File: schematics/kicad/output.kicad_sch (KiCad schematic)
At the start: 33 parts, among them J7 DE15_Socket_HighDensity, K1300 10uF, U1 BT458, U1300 HM53461, U1301 HM53461, U1302 HM53461, U1303 HM53461, U1304 HM53461, U1305 HM53461, U1306 HM53461, U1307 HM53461, U1311 92.9405Mhz, U1314 10H350, U1315 LM385BZ-1.2, U1318 74F08, U2 10H101, U3 10H131

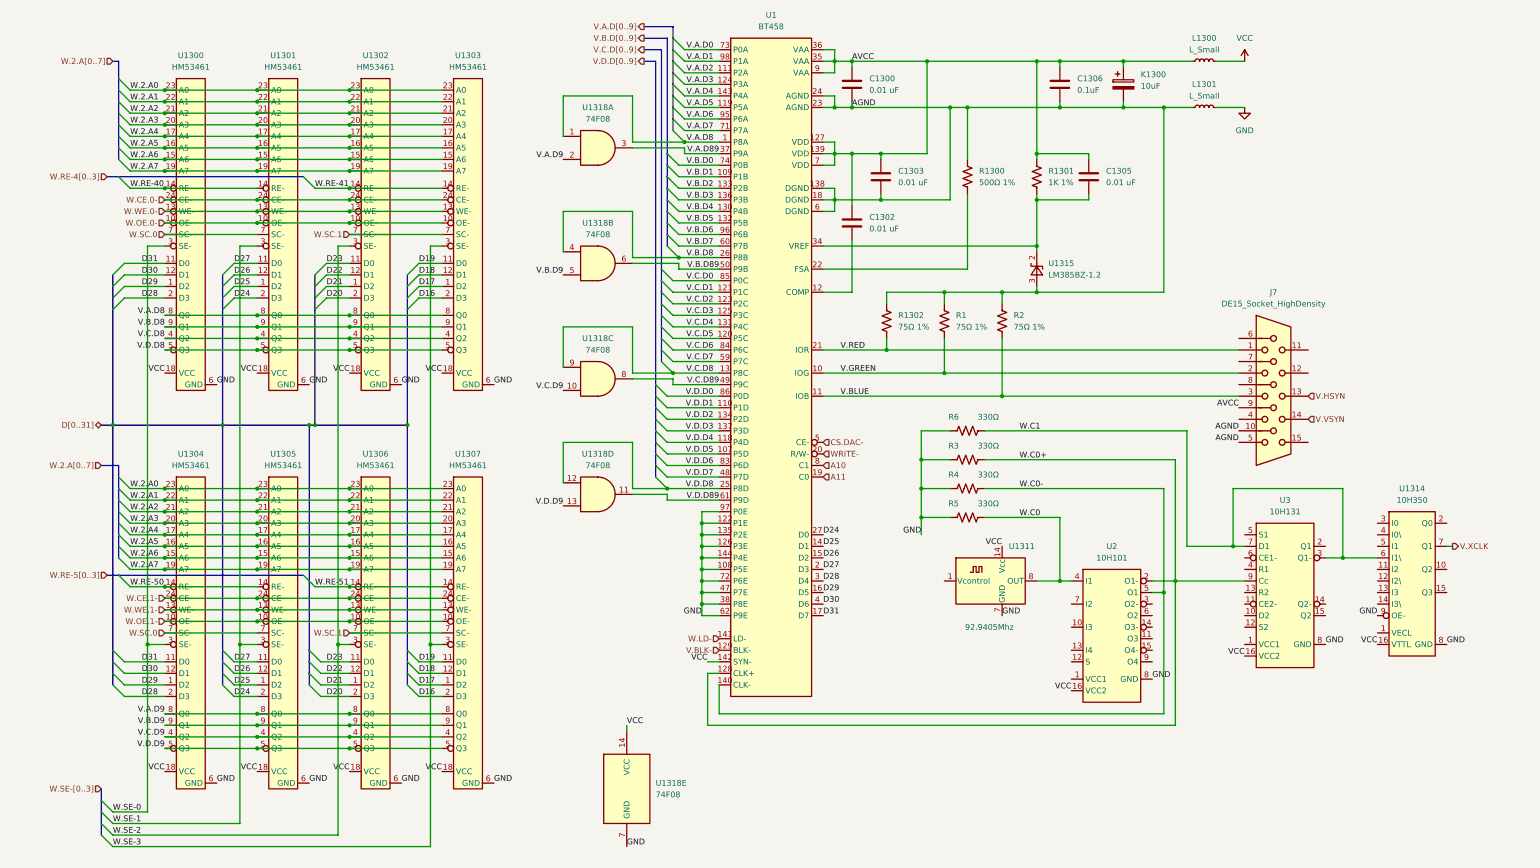
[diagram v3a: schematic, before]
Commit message: First initial layout, fix ZIP footprint.
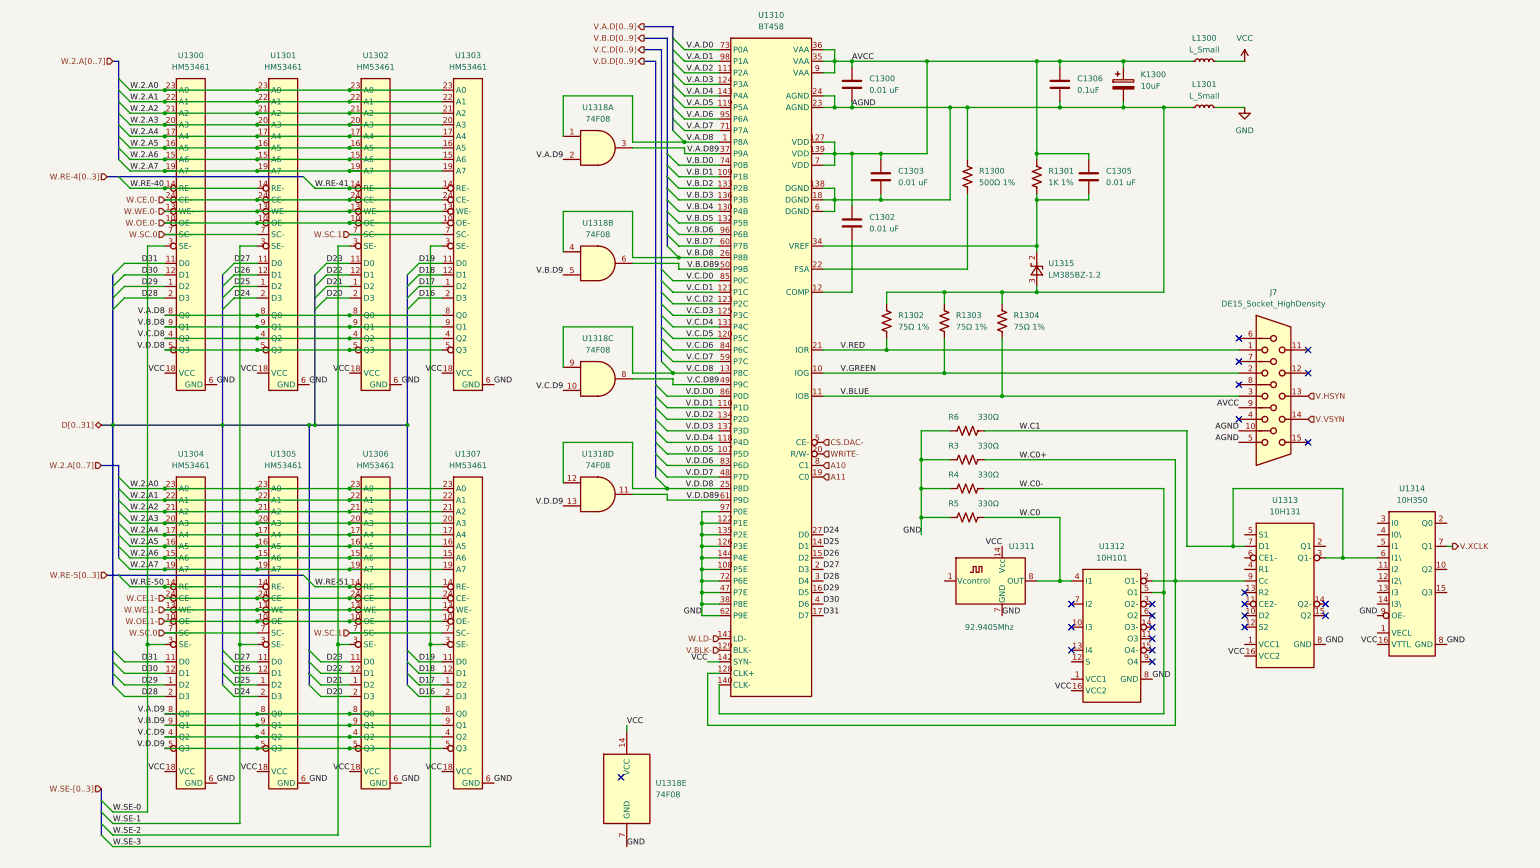
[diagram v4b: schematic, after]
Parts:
- C1300, C1302, C1303, C1305, C1306: footprint (none) -> Capacitor_THT:C_Rect_L7.0mm_W2.0mm_P5.00mm
- J7: footprint (none) -> Connector_Dsub:DSUB-15-HD_Socket_Horizontal_P2.29x2.54mm_EdgePinOffset8.35mm_Housed_MountingHolesOffset10.89mm
- K1300: footprint (none) -> Capacitor_THT:CP_Radial_D10.0mm_P5.00mm
- L1300, L1301: footprint (none) -> Resistor_THT:R_Axial_DIN0309_L9.0mm_D3.2mm_P12.70mm_Horizontal
- R1300, R1301, R1302, R3, R4, R5, R6: footprint (none) -> Resistor_THT:R_Axial_DIN0207_L6.3mm_D2.5mm_P10.16mm_Horizontal
- R1303: renamed from R1; footprint (none) -> Resistor_THT:R_Axial_DIN0207_L6.3mm_D2.5mm_P10.16mm_Horizontal
- R1304: renamed from R2; footprint (none) -> Resistor_THT:R_Axial_DIN0207_L6.3mm_D2.5mm_P10.16mm_Horizontal
- U1318: footprint (none) -> Package_DIP:DIP-14_W7.62mm
- renumbered U1 to U1310, U2 to U1312, U3 to U1313
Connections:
- no-connect marks 0 -> 23
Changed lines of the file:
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@@
 		(color 0 0 0 0)
 	)
+	(no_connect
+		(at 279.4 95.25)
+	)
+	(no_connect
+		(at 280.67 146.05)
+	)
+	(no_connect
+		(at 280.67 140.97)
+	)
+	(no_connect
+		(at 242.57 148.59)
+	)
+	(no_connect
+		(at 260.35 143.51)
+	)
+	(no_connect
+		(at 294.64 107.95)
+	)
+	(no_connect
+		(at 280.67 148.59)
+	)
+	(no_connect
+		(at 294.64 87.63)
+	)
+	(no_connect
+		(at 143.51 181.61)
+	)
+	(no_connect
+		(at 260.35 146.05)
+	)
+	(no_connect
+		(at 260.35 151.13)
+	)
+	(no_connect
+		(at 260.35 148.59)
+	)
+	(no_connect
+		(at 260.35 153.67)
+	)
+	(no_connect
+		(at 260.35 156.21)
+	)
+	(no_connect
+		(at 298.45 146.05)
+	)
+	(no_connect
+		(at 280.67 143.51)
+	)
+	(no_connect
+		(at 294.64 92.71)
+	)
+	(no_connect
+		(at 242.57 143.51)
+	)
+	(no_connect
+		(at 242.57 153.67)
+	)
+	(no_connect
+		(at 279.4 90.17)
+	)
+	(no_connect
+		(at 279.4 85.09)
+	)
+	(no_connect
+		(at 279.4 102.87)
+	)
+	(no_connect
+		(at 298.45 143.51)
+	)
 	(bus_entry
 		(at 33.02 40.64)
@@
 			)
 		)
-		(property "Footprint" ""
+		(property "Footprint" "Package_DIP:DIP-14_W7.62mm"
 			(at 138.43 119.38 0)
 			(effects
@@
 			)
 		)
-		(property "Footprint" ""
+		(property "Footprint" "Resistor_THT:R_Axial_DIN0207_L6.3mm_D2.5mm_P10.16mm_Horizontal"
 			(at 202.946 81.534 90)
 			(effects
@@
 		(dnp no)
 		(fields_autoplaced yes)
-		(property "Reference" "U1"
+		(property "Reference" "U1310"
 			(at 176.53 13.97 0)
 			(effects
@@
 			(project ""
 				(path "/7c2b6a13-c303-4adb-8eed-6e6a9ac5307e/29ede95e-baf3-44af-bd6e-b3be323fd399"
-					(reference "U1")
+					(reference "U1310")
 					(unit 1)
 				)
@@
 			)
 		)
-		(property "Footprint" ""
+		(property "Footprint" "Resistor_THT:R_Axial_DIN0309_L9.0mm_D3.2mm_P12.70mm_Horizontal"
 			(at 271.78 34.29 0)
 			(effects
@@
 			)
 		)
-		(property "Footprint" ""
+		(property "Footprint" "Resistor_THT:R_Axial_DIN0207_L6.3mm_D2.5mm_P10.16mm_Horizontal"
 			(at 219.964 117.094 90)
 			(effects
@@
 			)
 		)
-		(property "Footprint" ""
+		(property "Footprint" "Package_DIP:DIP-14_W7.62mm"
 			(at 138.43 43.18 0)
 			(effects
@@
 			)
 		)
-		(property "Footprint" ""
+		(property "Footprint" "Resistor_THT:R_Axial_DIN0309_L9.0mm_D3.2mm_P12.70mm_Horizontal"
 			(at 271.78 24.13 0)
 			(effects
@@
 			)
 		)
-		(property "Footprint" ""
+		(property "Footprint" "Capacitor_THT:C_Rect_L7.0mm_W2.0mm_P5.00mm"
 			(at 247.3452 53.34 0)
 			(effects
@@
 			)
 		)
-		(property "Footprint" ""
+		(property "Footprint" "Resistor_THT:R_Axial_DIN0207_L6.3mm_D2.5mm_P10.16mm_Horizontal"
 			(at 235.966 49.784 90)
 			(effects
@@
 			)
 		)
-		(property "Footprint" ""
+		(property "Footprint" "Capacitor_THT:C_Rect_L7.0mm_W2.0mm_P5.00mm"
 			(at 195.2752 33.02 0)
 			(effects
@@
 			)
 		)
-		(property "Footprint" ""
+		(property "Footprint" "Capacitor_THT:CP_Radial_D10.0mm_P5.00mm"
 			(at 254.9652 33.02 0)
 			(effects
@@
 			)
 		)
-		(property "Footprint" ""
+		(property "Footprint" "Capacitor_THT:C_Rect_L7.0mm_W2.0mm_P5.00mm"
 			(at 201.6252 53.34 0)
 			(effects
@@
 		(on_board yes)
 		(dnp no)
-		(property "Reference" "R1"
+		(property "Reference" "R1303"
 			(at 217.17 80.0099 0)
 			(effects
@@
 			)
 		)
-		(property "Footprint" ""
+		(property "Footprint" "Resistor_THT:R_Axial_DIN0207_L6.3mm_D2.5mm_P10.16mm_Horizontal"
 			(at 215.646 81.534 90)
 			(effects
@@
 			(project "cg4"
 				(path "/7c2b6a13-c303-4adb-8eed-6e6a9ac5307e/29ede95e-baf3-44af-bd6e-b3be323fd399"
-					(reference "R1")
+					(reference "R1303")
 					(unit 1)
 				)
@@
 			)
 		)
-		(property "Footprint" ""
+		(property "Footprint" "Capacitor_THT:C_Rect_L7.0mm_W2.0mm_P5.00mm"
 			(at 240.9952 33.02 0)
 			(effects
@@
 			)
 		)
-		(property "Footprint" ""
+		(property "Footprint" "Resistor_THT:R_Axial_DIN0207_L6.3mm_D2.5mm_P10.16mm_Horizontal"
 			(at 219.964 104.394 90)
 			(effects
@@
 		(dnp no)
 		(fields_autoplaced yes)
-		(property "Reference" "R2"
+		(property "Reference" "R1304"
 			(at 229.87 80.0099 0)
 			(effects
@@
 			)
 		)
-		(property "Footprint" ""
+		(property "Footprint" "Resistor_THT:R_Axial_DIN0207_L6.3mm_D2.5mm_P10.16mm_Horizontal"
 			(at 228.346 81.534 90)
 			(effects
@@
 			(project "cg4"
 				(path "/7c2b6a13-c303-4adb-8eed-6e6a9ac5307e/29ede95e-baf3-44af-bd6e-b3be323fd399"
-					(reference "R2")
+					(reference "R1304")
 					(unit 1)
 				)
@@
 		(dnp no)
 		(fields_autoplaced yes)
-		(property "Reference" "U2"
+		(property "Reference" "U1312"
 			(at 251.46 130.81 0)
 			(effects
@@
 			(project ""
 				(path "/7c2b6a13-c303-4adb-8eed-6e6a9ac5307e/29ede95e-baf3-44af-bd6e-b3be323fd399"
-					(reference "U2")
+					(reference "U1312")
 					(unit 1)
 				)
@@
 			)
 		)
-		(property "Footprint" ""
+		(property "Footprint" "Resistor_THT:R_Axial_DIN0207_L6.3mm_D2.5mm_P10.16mm_Horizontal"
 			(at 220.726 49.784 90)
 			(effects
@@
 			)
 		)
-		(property "Footprint" ""
+		(property "Footprint" "Connector_Dsub:DSUB-15-HD_Socket_Horizontal_P2.29x2.54mm_EdgePinOffset8.35mm_Housed_MountingHolesOffset10.89mm"
 			(at 262.89 87.63 0)
 			(effects
@@
 			)
 		)
-		(property "Footprint" ""
+		(property "Footprint" "Resistor_THT:R_Axial_DIN0207_L6.3mm_D2.5mm_P10.16mm_Horizontal"
 			(at 219.964 123.444 90)
 			(effects
@@
 			)
 		)
-		(property "Footprint" ""
+		(property "Footprint" "Resistor_THT:R_Axial_DIN0207_L6.3mm_D2.5mm_P10.16mm_Horizontal"
 			(at 219.964 110.744 90)
 			(effects
@@
 			)
 		)
-		(property "Footprint" ""
+		(property "Footprint" "Package_DIP:DIP-14_W7.62mm"
 			(at 144.78 184.15 0)
 			(effects
@@
 		(dnp no)
 		(fields_autoplaced yes)
-		(property "Reference" "U3"
+		(property "Reference" "U1313"
 			(at 289.56 120.65 0)
 			(effects
@@
 			(project ""
 				(path "/7c2b6a13-c303-4adb-8eed-6e6a9ac5307e/29ede95e-baf3-44af-bd6e-b3be323fd399"
-					(reference "U3")
+					(reference "U1313")
 					(unit 1)
 				)
@@
 			)
 		)
-		(property "Footprint" ""
+		(property "Footprint" "Package_DIP:DIP-14_W7.62mm"
 			(at 138.43 68.58 0)
 			(effects
@@
 			)
 		)
-		(property "Footprint" ""
+		(property "Footprint" "Package_DIP:DIP-14_W7.62mm"
 			(at 138.43 93.98 0)
 			(effects
@@
 			)
 		)
-		(property "Footprint" ""
+		(property "Footprint" "Capacitor_THT:C_Rect_L7.0mm_W2.0mm_P5.00mm"
 			(at 195.2752 63.5 0)
 			(effects
